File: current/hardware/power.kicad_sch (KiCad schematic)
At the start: 22 parts, among them J1 2P PUSH 3.5mm, Q1 AO4485, U1 LMR51420XDDCR, U2 AP2112K-3.3

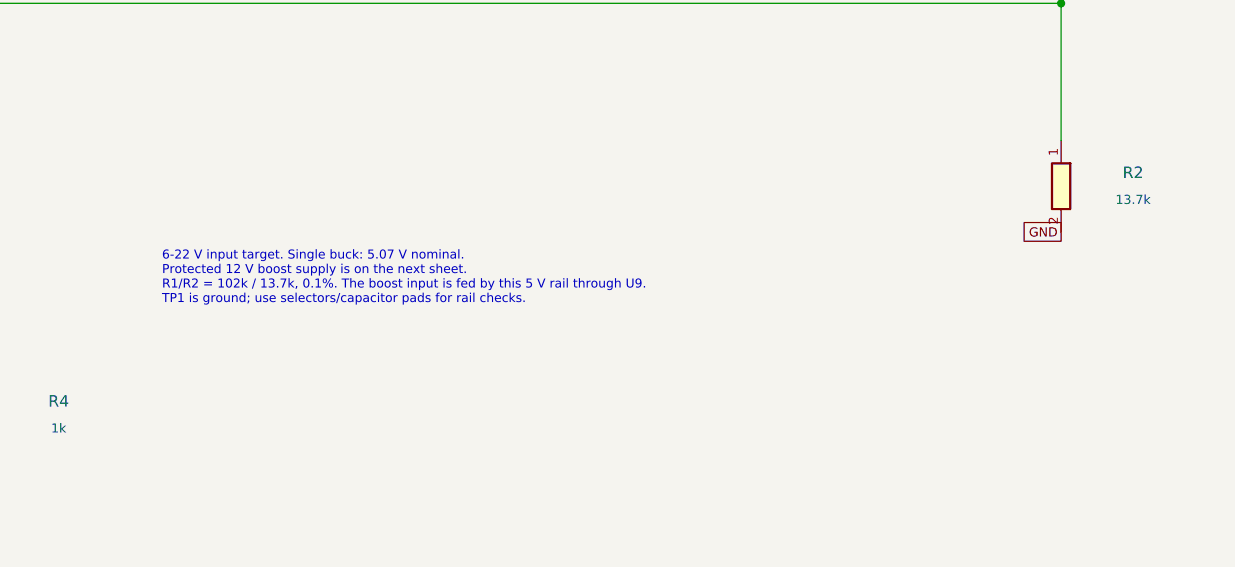
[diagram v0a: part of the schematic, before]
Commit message: Rev G: protect sensor power and verify startup and fault recovery
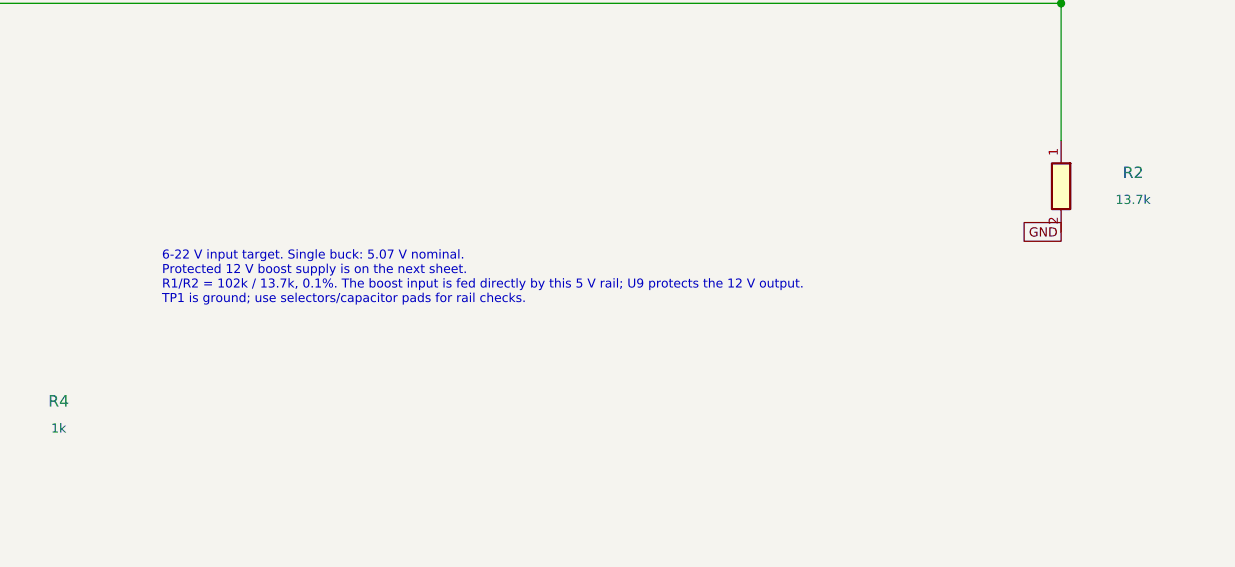
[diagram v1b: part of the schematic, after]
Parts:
- C7, C8: Notes Rev F sourcing substitution: value, dielectric, voltage, to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 -> Retained sourcing substitution: value, dielectric, voltage,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
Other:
- note added: "6-22 V input target. Single buck: 5.07 V nominal. Protected 12 V boost supply is on the next sheet. R1/R2 = 102k / 13.7k, 0.1%. The boost input is fed directly by this 5 V rail; U9 protects the 12 V output. TP1 is ground; use selectors/capacitor pads for rail checks."
- note removed: "6-22 V input target. Single buck: 5.07 V nominal. Protected 12 V boost supply is on the next sheet. R1/R2 = 102k / 13.7k, 0.1%. The boost input is fed by this 5 V rail through U9. TP1 is ground; use selectors/capacitor pads for rail checks."
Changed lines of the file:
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@@
 (kicad_sch (version 20250114) (generator "eeschema") (paper "A3")
-(title_block (title "SC12 - Battery entry and internal supplies") (date "2026-09-08") (rev "F") (company "Original sensor interface design") (comment 1 "Prototype: bench validation required before robot use"))
+(title_block (title "SC12 - Battery entry and internal supplies") (date "2026-09-09") (rev "G") (company "Original sensor interface design") (comment 1 "Prototype: bench validation required before robot use"))
 (text "Battery entry and internal supplies" (at 15 15 0) (effects (font (size 2.54 2.54)) (justify left top)))
 (text "PROTECTED BATTERY ENTRY" (at 15 28 0) (effects (font (size 1.8 1.8)) (justify left top)))
@@
 (no_connect (at 121.92 270.51))
 (symbol (lib_id "FRC_Sensor_CAN:LDO") (at 106.68 269.24 0) (unit 1) (in_bom yes) (on_board yes) (dnp no) (property "Reference" "U2" (at 106.68 261.47 0) (effects (font (size 1.27 1.27))))(property "Value" "AP2112K-3.3" (at 106.68 263.97 0) (effects (font (size 1.016 1.016))))(property "Footprint" "FRC_Sensor_CAN:SOT-23-5" (at 106.68 269.24 0) (effects (font (size 1.27 1.27)) (hide yes)))(property "Datasheet" "" (at 106.68 269.24 0) (effects (font (size 1.27 1.27)) (hide yes)))(property "MPN" "AP2112K-3.3TRG1" (at 106.68 269.24 0) (effects (font (size 1.27 1.27)) (hide yes)))(property "Notes" "" (at 106.68 269.24 0) (effects (font (size 1.27 1.27)) (hide yes)))(pin "1")(pin "3")(pin "5")(pin "4")(pin "2")(instances (project "FRC_Sensor_CAN" (path "/32fd904d-6274-5c4e-88d3-bb1b48cbb6d1/fb3c0a9e-b322-5632-9eb0-a957beaadad4" (reference "U2") (unit 1)))) )
-(symbol (lib_id "FRC_Sensor_CAN:C") (at 50.8 264.16 270) (unit 1) (in_bom yes) (on_board yes) (dnp no) (property "Reference" "C7" (at 58.8 262.66 90) (effects (font (size 1.27 1.27))))(property "Value" "1uF" (at 58.8 265.66 90) (effects (font (size 1.016 1.016))))(property "Footprint" "FRC_Sensor_CAN:C_0805_2012Metric" (at 50.8 264.16 0) (effects (font (size 1.27 1.27)) (hide yes)))(property "Datasheet" "" (at 50.8 264.16 0) (effects (font (size 1.27 1.27)) (hide yes)))(property "MPN" "CL21B105KBFNNNE" (at 50.8 264.16 0) (effects (font (size 1.27 1.27)) (hide yes)))(property "Notes" "Rev F sourcing substitution: value, dielectric, voltage, tolerance and footprint retained; assess effective capacitance." (at 50.8 264.16 0) (effects (font (size 1.27 1.27)) (hide yes)))(pin "1")(pin "2")(instances (project "FRC_Sensor_CAN" (path "/32fd904d-6274-5c4e-88d3-bb1b48cbb6d1/fb3c0a9e-b322-5632-9eb0-a957beaadad4" (reference "C7") (unit 1)))) )
-(symbol (lib_id "FRC_Sensor_CAN:C") (at 170.18 264.16 270) (unit 1) (in_bom yes) (on_board yes) (dnp no) (property "Reference" "C8" (at 178.18 262.66 90) (effects (font (size 1.27 1.27))))(property "Value" "4.7uF" (at 178.18 265.66 90) (effects (font (size 1.016 1.016))))(property "Footprint" "FRC_Sensor_CAN:C_0805_2012Metric" (at 170.18 264.16 0) (effects (font (size 1.27 1.27)) (hide yes)))(property "Datasheet" "" (at 170.18 264.16 0) (effects (font (size 1.27 1.27)) (hide yes)))(property "MPN" "CL21B475KAFNNNE" (at 170.18 264.16 0) (effects (font (size 1.27 1.27)) (hide yes)))(property "Notes" "Rev F sourcing substitution: value, dielectric, voltage, tolerance and footprint retained; assess effective capacitance." (at 170.18 264.16 0) (effects (font (size 1.27 1.27)) (hide yes)))(pin "1")(pin "2")(instances (project "FRC_Sensor_CAN" (path "/32fd904d-6274-5c4e-88d3-bb1b48cbb6d1/fb3c0a9e-b322-5632-9eb0-a957beaadad4" (reference "C8") (unit 1)))) )
+(symbol (lib_id "FRC_Sensor_CAN:C") (at 50.8 264.16 270) (unit 1) (in_bom yes) (on_board yes) (dnp no) (property "Reference" "C7" (at 58.8 262.66 90) (effects (font (size 1.27 1.27))))(property "Value" "1uF" (at 58.8 265.66 90) (effects (font (size 1.016 1.016))))(property "Footprint" "FRC_Sensor_CAN:C_0805_2012Metric" (at 50.8 264.16 0) (effects (font (size 1.27 1.27)) (hide yes)))(property "Datasheet" "" (at 50.8 264.16 0) (effects (font (size 1.27 1.27)) (hide yes)))(property "MPN" "CL21B105KBFNNNE" (at 50.8 264.16 0) (effects (font (size 1.27 1.27)) (hide yes)))(property "Notes" "Retained sourcing substitution: value, dielectric, voltage, tolerance and footprint retained; assess effective capacitance." (at 50.8 264.16 0) (effects (font (size 1.27 1.27)) (hide yes)))(pin "1")(pin "2")(instances (project "FRC_Sensor_CAN" (path "/32fd904d-6274-5c4e-88d3-bb1b48cbb6d1/fb3c0a9e-b322-5632-9eb0-a957beaadad4" (reference "C7") (unit 1)))) )
+(symbol (lib_id "FRC_Sensor_CAN:C") (at 170.18 264.16 270) (unit 1) (in_bom yes) (on_board yes) (dnp no) (property "Reference" "C8" (at 178.18 262.66 90) (effects (font (size 1.27 1.27))))(property "Value" "4.7uF" (at 178.18 265.66 90) (effects (font (size 1.016 1.016))))(property "Footprint" "FRC_Sensor_CAN:C_0805_2012Metric" (at 170.18 264.16 0) (effects (font (size 1.27 1.27)) (hide yes)))(property "Datasheet" "" (at 170.18 264.16 0) (effects (font (size 1.27 1.27)) (hide yes)))(property "MPN" "CL21B475KAFNNNE" (at 170.18 264.16 0) (effects (font (size 1.27 1.27)) (hide yes)))(property "Notes" "Retained sourcing substitution: value, dielectric, voltage, tolerance and footprint retained; assess effective capacitance." (at 170.18 264.16 0) (effects (font (size 1.27 1.27)) (hide yes)))(pin "1")(pin "2")(instances (project "FRC_Sensor_CAN" (path "/32fd904d-6274-5c4e-88d3-bb1b48cbb6d1/fb3c0a9e-b322-5632-9eb0-a957beaadad4" (reference "C8") (unit 1)))) )
 (symbol (lib_id "FRC_Sensor_CAN:R") (at 223.52 264.16 270) (unit 1) (in_bom yes) (on_board yes) (dnp no) (property "Reference" "R4" (at 231.52 262.66 90) (effects (font (size 1.27 1.27))))(property "Value" "1k" (at 231.52 265.66 90) (effects (font (size 1.016 1.016))))(property "Footprint" "FRC_Sensor_CAN:R_0805_2012Metric" (at 223.52 264.16 0) (effects (font (size 1.27 1.27)) (hide yes)))(property "Datasheet" "" (at 223.52 264.16 0) (effects (font (size 1.27 1.27)) (hide yes)))(property "MPN" "0805W8F1001T5E" (at 223.52 264.16 0) (effects (font (size 1.27 1.27)) (hide yes)))(property "Notes" "3V3 bleed retained for conservative powered-off leakage budget; 3.3 mA load." (at 223.52 264.16 0) (effects (font (size 1.27 1.27)) (hide yes)))(pin "1")(pin "2")(instances (project "FRC_Sensor_CAN" (path "/32fd904d-6274-5c4e-88d3-bb1b48cbb6d1/fb3c0a9e-b322-5632-9eb0-a957beaadad4" (reference "R4") (unit 1)))) )
 (global_label "V5_INTERNAL" (shape passive) (at 91.44 267.97 0) (effects (font (size 1.016 1.016)) (justify right)) (property "Intersheetrefs" "${INTERSHEET_REFS}" (at 91.44 267.97 0) (effects (font (size 1.27 1.27)) (hide yes))))
@@
 (global_label "V5_INTERNAL" (shape passive) (at 375.92 243.84 0) (effects (font (size 1.016 1.016)) (justify right)) (property "Intersheetrefs" "${INTERSHEET_REFS}" (at 375.92 243.84 0) (effects (font (size 1.27 1.27)) (hide yes))))
 (symbol (lib_id "FRC_Sensor_CAN:PWR_FLAG") (at 375.92 236.22 0) (unit 1) (in_bom no) (on_board yes) (dnp no) (property "Reference" "#FLG03" (at 375.92 229.72 0) (effects (font (size 1.27 1.27))))(property "Value" "PWR_FLAG" (at 375.92 232.22 0) (effects (font (size 1.016 1.016))))(property "Footprint" "" (at 375.92 236.22 0) (effects (font (size 1.27 1.27)) (hide yes)))(property "Datasheet" "" (at 375.92 236.22 0) (effects (font (size 1.27 1.27)) (hide yes)))(property "MPN" "" (at 375.92 236.22 0) (effects (font (size 1.27 1.27)) (hide yes)))(property "Notes" "" (at 375.92 236.22 0) (effects (font (size 1.27 1.27)) (hide yes)))(pin "1")(instances (project "FRC_Sensor_CAN" (path "/32fd904d-6274-5c4e-88d3-bb1b48cbb6d1/fb3c0a9e-b322-5632-9eb0-a957beaadad4" (reference "#FLG03") (unit 1)))) )
-(text "6-22 V input target. Single buck: 5.07 V nominal.\nProtected 12 V boost supply is on the next sheet.\nR1/R2 = 102k / 13.7k, 0.1%. The boost input is fed by this 5 V rail through U9.\nTP1 is ground; use selectors/capacitor pads for rail checks." (at 243 246 0) (effects (font (size 1.0 1.0)) (justify left top)))
+(text "6-22 V input target. Single buck: 5.07 V nominal.\nProtected 12 V boost supply is on the next sheet.\nR1/R2 = 102k / 13.7k, 0.1%. The boost input is fed directly by this 5 V rail; U9 protects the 12 V output.\nTP1 is ground; use selectors/capacitor pads for rail checks." (at 243 246 0) (effects (font (size 1.0 1.0)) (justify left top)))
 (embedded_fonts no))

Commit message: Prepare factory SMT assembly with high-reflow C1 and exact MCU sourcing
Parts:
- C1: footprint FRC_Sensor_CAN:CP_Elec_8x6.5 -> FRC_Sensor_CAN:CP_Panasonic_FT_6.3x5.8; MPN EEE-FK1H470P -> EEEFT1H470AP; Notes (none) -> Factory fitted. 47uF 50V 20%; 195mA ripple, 0.68ohm max ESR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
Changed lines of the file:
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@@
 (junction (at 167.64 57.15) (diameter 0) (color 0 0 0 0))
 (global_label "GND" (shape passive) (at 167.64 86.36 0) (effects (font (size 1.016 1.016)) (justify right)) (property "Intersheetrefs" "${INTERSHEET_REFS}" (at 167.64 86.36 0) (effects (font (size 1.27 1.27)) (hide yes))))
-(symbol (lib_id "FRC_Sensor_CAN:CP") (at 218.44 81.28 270) (unit 1) (in_bom yes) (on_board yes) (dnp no) (property "Reference" "C1" (at 226.44 79.78 90) (effects (font (size 1.27 1.27))))(property "Value" "47uF" (at 226.44 82.78 90) (effects (font (size 1.016 1.016))))(property "Footprint" "FRC_Sensor_CAN:CP_Elec_8x6.5" (at 218.44 81.28 0) (effects (font (size 1.27 1.27)) (hide yes)))(property "Datasheet" "" (at 218.44 81.28 0) (effects (font (size 1.27 1.27)) (hide yes)))(property "MPN" "EEE-FK1H470P" (at 218.44 81.28 0) (effects (font (size 1.27 1.27)) (hide yes)))(property "Notes" "" (at 218.44 81.28 0) (effects (font (size 1.27 1.27)) (hide yes)))(pin "1")(pin "2")(instances (project "FRC_Sensor_CAN" (path "/32fd904d-6274-5c4e-88d3-bb1b48cbb6d1/fb3c0a9e-b322-5632-9eb0-a957beaadad4" (reference "C1") (unit 1)))) )
+(symbol (lib_id "FRC_Sensor_CAN:CP") (at 218.44 81.28 270) (unit 1) (in_bom yes) (on_board yes) (dnp no) (property "Reference" "C1" (at 226.44 79.78 90) (effects (font (size 1.27 1.27))))(property "Value" "47uF" (at 226.44 82.78 90) (effects (font (size 1.016 1.016))))(property "Footprint" "FRC_Sensor_CAN:CP_Panasonic_FT_6.3x5.8" (at 218.44 81.28 0) (effects (font (size 1.27 1.27)) (hide yes)))(property "Datasheet" "" (at 218.44 81.28 0) (effects (font (size 1.27 1.27)) (hide yes)))(property "MPN" "EEEFT1H470AP" (at 218.44 81.28 0) (effects (font (size 1.27 1.27)) (hide yes)))(property "Notes" "Factory fitted. 47uF 50V 20%; 195mA ripple, 0.68ohm max ESR. Panasonic profile (5); respect dwell limits." (at 218.44 81.28 0) (effects (font (size 1.27 1.27)) (hide yes)))(pin "1")(pin "2")(instances (project "FRC_Sensor_CAN" (path "/32fd904d-6274-5c4e-88d3-bb1b48cbb6d1/fb3c0a9e-b322-5632-9eb0-a957beaadad4" (reference "C1") (unit 1)))) )
 (wire (pts (xy 218.44 57.15) (xy 218.44 76.2)) (stroke (width 0) (type default)))
 (junction (at 218.44 57.15) (diameter 0) (color 0 0 0 0))

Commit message: Snapshot current Rev H design for isolated compact-board work
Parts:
- L1: value 10uH -> 8.2uH; MPN SRP7028A-100M -> SRP7028A-8R2M; Notes 3.5A RMS, 6A saturation; use specified family, not NRND SRP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 -> 4A RMS, 7.5A saturation; paired with 3A LMR51430. Use speci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
- U1: value LMR51420XDDCR -> LMR51430XDDCR; MPN LMR51420XDDCR -> LMR51430XDDCR
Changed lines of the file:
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@@
 (symbol (lib_id "FRC_Sensor_CAN:TP") (at 50.8 114.3 0) (unit 1) (in_bom no) (on_board yes) (dnp no) (property "Reference" "TP1" (at 50.8 107.8 0) (effects (font (size 1.27 1.27))))(property "Value" "GND" (at 50.8 110.3 0) (effects (font (size 1.016 1.016))))(property "Footprint" "FRC_Sensor_CAN:TestPoint_Pad_D2.0mm" (at 50.8 114.3 0) (effects (font (size 1.27 1.27)) (hide yes)))(property "Datasheet" "" (at 50.8 114.3 0) (effects (font (size 1.27 1.27)) (hide yes)))(property "MPN" "" (at 50.8 114.3 0) (effects (font (size 1.27 1.27)) (hide yes)))(property "Notes" "Bare PCB test pad; excluded from purchased BOM." (at 50.8 114.3 0) (effects (font (size 1.27 1.27)) (hide yes)))(pin "1")(instances (project "FRC_Sensor_CAN" (path "/32fd904d-6274-5c4e-88d3-bb1b48cbb6d1/fb3c0a9e-b322-5632-9eb0-a957beaadad4" (reference "TP1") (unit 1)))) )
 (text "500 kHz BUCK / REGULATED 5 V" (at 15 130 0) (effects (font (size 1.8 1.8)) (justify left top)))
-(symbol (lib_id "FRC_Sensor_CAN:BUCK") (at 101.6 167.64000000000001 0) (unit 1) (in_bom yes) (on_board yes) (dnp no) (property "Reference" "U1" (at 101.6 158.6 0) (effects (font (size 1.27 1.27))))(property "Value" "LMR51420XDDCR" (at 101.6 161.1 0) (effects (font (size 1.016 1.016))))(property "Footprint" "FRC_Sensor_CAN:TSOT-23-6" (at 101.6 167.64 0) (effects (font (size 1.27 1.27)) (hide yes)))(property "Datasheet" "" (at 101.6 167.64 0) (effects (font (size 1.27 1.27)) (hide yes)))(property "MPN" "LMR51420XDDCR" (at 101.6 167.64 0) (effects (font (size 1.27 1.27)) (hide yes)))(property "Notes" "" (at 101.6 167.64 0) (effects (font (size 1.27 1.27)) (hide yes)))(pin "3")(pin "5")(pin "6")(pin "2")(pin "4")(pin "1")(instances (project "FRC_Sensor_CAN" (path "/32fd904d-6274-5c4e-88d3-bb1b48cbb6d1/fb3c0a9e-b322-5632-9eb0-a957beaadad4" (reference "U1") (unit 1)))) )
-(symbol (lib_id "FRC_Sensor_CAN:L") (at 187.96 167.64000000000001 0) (unit 1) (in_bom yes) (on_board yes) (dnp no) (property "Reference" "L1" (at 187.96 161.14 0) (effects (font (size 1.27 1.27))))(property "Value" "10uH" (at 187.96 163.64 0) (effects (font (size 1.016 1.016))))(property "Footprint" "FRC_Sensor_CAN:L_Bourns_SRP7028A_7.3x6.6mm" (at 187.96 167.64 0) (effects (font (size 1.27 1.27)) (hide yes)))(property "Datasheet" "" (at 187.96 167.64 0) (effects (font (size 1.27 1.27)) (hide yes)))(property "MPN" "SRP7028A-100M" (at 187.96 167.64 0) (effects (font (size 1.27 1.27)) (hide yes)))(property "Notes" "3.5A RMS, 6A saturation; use specified family, not NRND SRP7030." (at 187.96 167.64 0) (effects (font (size 1.27 1.27)) (hide yes)))(pin "1")(pin "2")(instances (project "FRC_Sensor_CAN" (path "/32fd904d-6274-5c4e-88d3-bb1b48cbb6d1/fb3c0a9e-b322-5632-9eb0-a957beaadad4" (reference "L1") (unit 1)))) )
+(symbol (lib_id "FRC_Sensor_CAN:BUCK") (at 101.6 167.64000000000001 0) (unit 1) (in_bom yes) (on_board yes) (dnp no) (property "Reference" "U1" (at 101.6 158.6 0) (effects (font (size 1.27 1.27))))(property "Value" "LMR51430XDDCR" (at 101.6 161.1 0) (effects (font (size 1.016 1.016))))(property "Footprint" "FRC_Sensor_CAN:TSOT-23-6" (at 101.6 167.64 0) (effects (font (size 1.27 1.27)) (hide yes)))(property "Datasheet" "" (at 101.6 167.64 0) (effects (font (size 1.27 1.27)) (hide yes)))(property "MPN" "LMR51430XDDCR" (at 101.6 167.64 0) (effects (font (size 1.27 1.27)) (hide yes)))(property "Notes" "" (at 101.6 167.64 0) (effects (font (size 1.27 1.27)) (hide yes)))(pin "3")(pin "5")(pin "6")(pin "2")(pin "4")(pin "1")(instances (project "FRC_Sensor_CAN" (path "/32fd904d-6274-5c4e-88d3-bb1b48cbb6d1/fb3c0a9e-b322-5632-9eb0-a957beaadad4" (reference "U1") (unit 1)))) )
+(symbol (lib_id "FRC_Sensor_CAN:L") (at 187.96 167.64000000000001 0) (unit 1) (in_bom yes) (on_board yes) (dnp no) (property "Reference" "L1" (at 187.96 161.14 0) (effects (font (size 1.27 1.27))))(property "Value" "8.2uH" (at 187.96 163.64 0) (effects (font (size 1.016 1.016))))(property "Footprint" "FRC_Sensor_CAN:L_Bourns_SRP7028A_7.3x6.6mm" (at 187.96 167.64 0) (effects (font (size 1.27 1.27)) (hide yes)))(property "Datasheet" "" (at 187.96 167.64 0) (effects (font (size 1.27 1.27)) (hide yes)))(property "MPN" "SRP7028A-8R2M" (at 187.96 167.64 0) (effects (font (size 1.27 1.27)) (hide yes)))(property "Notes" "4A RMS, 7.5A saturation; paired with 3A LMR51430. Use specified SRP7028A family." (at 187.96 167.64 0) (effects (font (size 1.27 1.27)) (hide yes)))(pin "1")(pin "2")(instances (project "FRC_Sensor_CAN" (path "/32fd904d-6274-5c4e-88d3-bb1b48cbb6d1/fb3c0a9e-b322-5632-9eb0-a957beaadad4" (reference "L1") (unit 1)))) )
 (symbol (lib_id "FRC_Sensor_CAN:C") (at 152.4 139.7 0) (unit 1) (in_bom yes) (on_board yes) (dnp no) (property "Reference" "C6" (at 152.4 133.2 0) (effects (font (size 1.27 1.27))))(property "Value" "100nF" (at 152.4 135.7 0) (effects (font (size 1.016 1.016))))(property "Footprint" "FRC_Sensor_CAN:C_0805_2012Metric" (at 152.4 139.7 0) (effects (font (size 1.27 1.27)) (hide yes)))(property "Datasheet" "" (at 152.4 139.7 0) (effects (font (size 1.27 1.27)) (hide yes)))(property "MPN" "CL21B104KCFNNNE" (at 152.4 139.7 0) (effects (font (size 1.27 1.27)) (hide yes)))(property "Notes" "" (at 152.4 139.7 0) (effects (font (size 1.27 1.27)) (hide yes)))(pin "1")(pin "2")(instances (project "FRC_Sensor_CAN" (path "/32fd904d-6274-5c4e-88d3-bb1b48cbb6d1/fb3c0a9e-b322-5632-9eb0-a957beaadad4" (reference "C6") (unit 1)))) )
 (wire (pts (xy 86.36 165.1) (xy 45.72 165.1)) (stroke (width 0) (type default)))
